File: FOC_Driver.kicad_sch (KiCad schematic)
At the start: 0 parts

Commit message: Wip
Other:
- removed sheet External_Power
- added sheet Encoder (Encoder.kicad_sch)
- added sheet External_Memory (External_Memory.kicad_sch)
- added sheet RS485 (RS485.kicad_sch)
- added sheet User_Interface (User_Interface.kicad_sch)
- sheet Connectors ports: added BypassRelay, Current_A, Current_B, Current_C, EM_STOP, PWM_AH, PWM_AL, PWM_BH, PWM_BL, PWM_CH, PWM_CL, SoftwareBrake, busVoltage, heatsinkTemperature; removed none
- sheet MCU ports: added BusVoltage, Bypass_Relay, Current_A, Current_B, Current_C, EM_STOP, Encoder_0, Encoder_A, Encoder_B, Encoder_En, Encoder_Flg, MISO, MOSI, RS485_Rx, RS485_Tx, SCLK, Software_Brake, heatsinkTemperature, nCS, nWP; removed none

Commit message: wip
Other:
- sheet Connectors ports: added Disable_Drive; removed EM_STOP
- sheet MCU ports: added Disable_Drive, ESTOP, PWM_AH, PWM_AL, PWM_BH, PWM_BL, PWM_CH, PWM_CL, RS485_DE; removed EM_STOP
- sheet RS485 ports: added RS485_DE; removed none

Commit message: wip
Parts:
- added TP1: TestPoint, TestPoint:TestPoint_Pad_D1.0mm, symbol Connector:TestPoint
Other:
- added sheet Power (Power.kicad_sch)

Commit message: 90% schematic first layout
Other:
- sheet External_Memory ports: added none; removed nWP
- sheet MCU ports: added ERROR_LED, ESTOP_LED, Error_Fixed, RUN_LED, RUN/STOP; removed nWP
- sheet User_Interface ports: added ERROR_LED, ESTOP_LED, Error_Fixed, Estop, RUN_LED, RUN/STOP; removed none
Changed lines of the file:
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@@
+	(wire
+		(pts
+			(xy 104.14 138.43) (xy 116.84 138.43)
+		)
+		(stroke
+			(width 0)
+			(type default)
+		)
+	)
 	(wire
 		(pts
@@
 	(wire
 		(pts
+			(xy 104.14 128.27) (xy 116.84 128.27)
+		)
+		(stroke
+			(width 0)
+			(type default)
+		)
+	)
+	(wire
+		(pts
 			(xy 160.02 85.09) (xy 182.88 85.09)
 		)
@@
 	(wire
 		(pts
-			(xy 160.02 133.35) (xy 182.88 133.35)
+			(xy 104.14 125.73) (xy 116.84 125.73)
 		)
 		(stroke
@@
 	(wire
 		(pts
+			(xy 104.14 140.97) (xy 116.84 140.97)
+		)
+		(stroke
+			(width 0)
+			(type default)
+		)
+	)
+	(wire
+		(pts
 			(xy 97.79 36.83) (xy 138.43 36.83)
 		)
@@
 	(wire
 		(pts
+			(xy 104.14 130.81) (xy 116.84 130.81)
+		)
+		(stroke
+			(width 0)
+			(type default)
+		)
+	)
+	(wire
+		(pts
 			(xy 97.79 46.99) (xy 128.27 46.99)
 		)
@@
 		(pts
 			(xy 102.87 87.63) (xy 116.84 87.63)
+		)
+		(stroke
+			(width 0)
+			(type default)
+		)
+	)
+	(wire
+		(pts
+			(xy 104.14 135.89) (xy 116.84 135.89)
 		)
 		(stroke
@@
 			)
 		)
-		(pin "nWP" input
-			(at 182.88 133.35 180)
-			(effects
-				(font
-					(size 1.27 1.27)
-				)
-				(justify left)
-			)
-		)
 		(pin "MISO" output
 			(at 182.88 135.89 180)
@@
 			)
 		)
-		(pin "nWP" output
-			(at 160.02 133.35 0)
-			(effects
-				(font
-					(size 1.27 1.27)
-				)
-				(justify right)
-			)
-		)
 		(pin "PWM_CH" output
 			(at 160.02 72.39 0)
@@
 		(pin "RS485_DE" output
 			(at 116.84 80.01 180)
+			(effects
+				(font
+					(size 1.27 1.27)
+				)
+				(justify left)
+			)
+		)
+		(pin "ERROR_LED" output
+			(at 116.84 125.73 180)
+			(effects
+				(font
+					(size 1.27 1.27)
+				)
+				(justify left)
+			)
+		)
+		(pin "RUN{slash}STOP" input
+			(at 116.84 138.43 180)
+			(effects
+				(font
+					(size 1.27 1.27)
+				)
+				(justify left)
+			)
+		)
+		(pin "ESTOP_LED" output
+			(at 116.84 130.81 180)
+			(effects
+				(font
+					(size 1.27 1.27)
+				)
+				(justify left)
+			)
+		)
+		(pin "RUN_LED" output
+			(at 116.84 128.27 180)
+			(effects
+				(font
+					(size 1.27 1.27)
+				)
+				(justify left)
+			)
+		)
+		(pin "Error_Fixed" input
+			(at 116.84 135.89 180)
 			(effects
 				(font
@@
 			)
 		)
+		(pin "Error_Fixed" output
+			(at 104.14 135.89 0)
+			(effects
+				(font
+					(size 1.27 1.27)
+				)
+				(justify right)
+			)
+		)
+		(pin "Estop" output
+			(at 104.14 140.97 0)
+			(effects
+				(font
+					(size 1.27 1.27)
+				)
+				(justify right)
+			)
+		)
+		(pin "RUN{slash}STOP" output
+			(at 104.14 138.43 0)
+			(effects
+				(font
+					(size 1.27 1.27)
+				)
+				(justify right)
+			)
+		)
+		(pin "ESTOP_LED" input
+			(at 104.14 130.81 0)
+			(effects
+				(font
+					(size 1.27 1.27)
+				)
+				(justify right)
+			)
+		)
+		(pin "RUN_LED" input
+			(at 104.14 128.27 0)
+			(effects
+				(font
+					(size 1.27 1.27)
+				)
+				(justify right)
+			)
+		)
+		(pin "ERROR_LED" input
+			(at 104.14 125.73 0)
+			(effects
+				(font
+					(size 1.27 1.27)
+				)
+				(justify right)
+			)
+		)

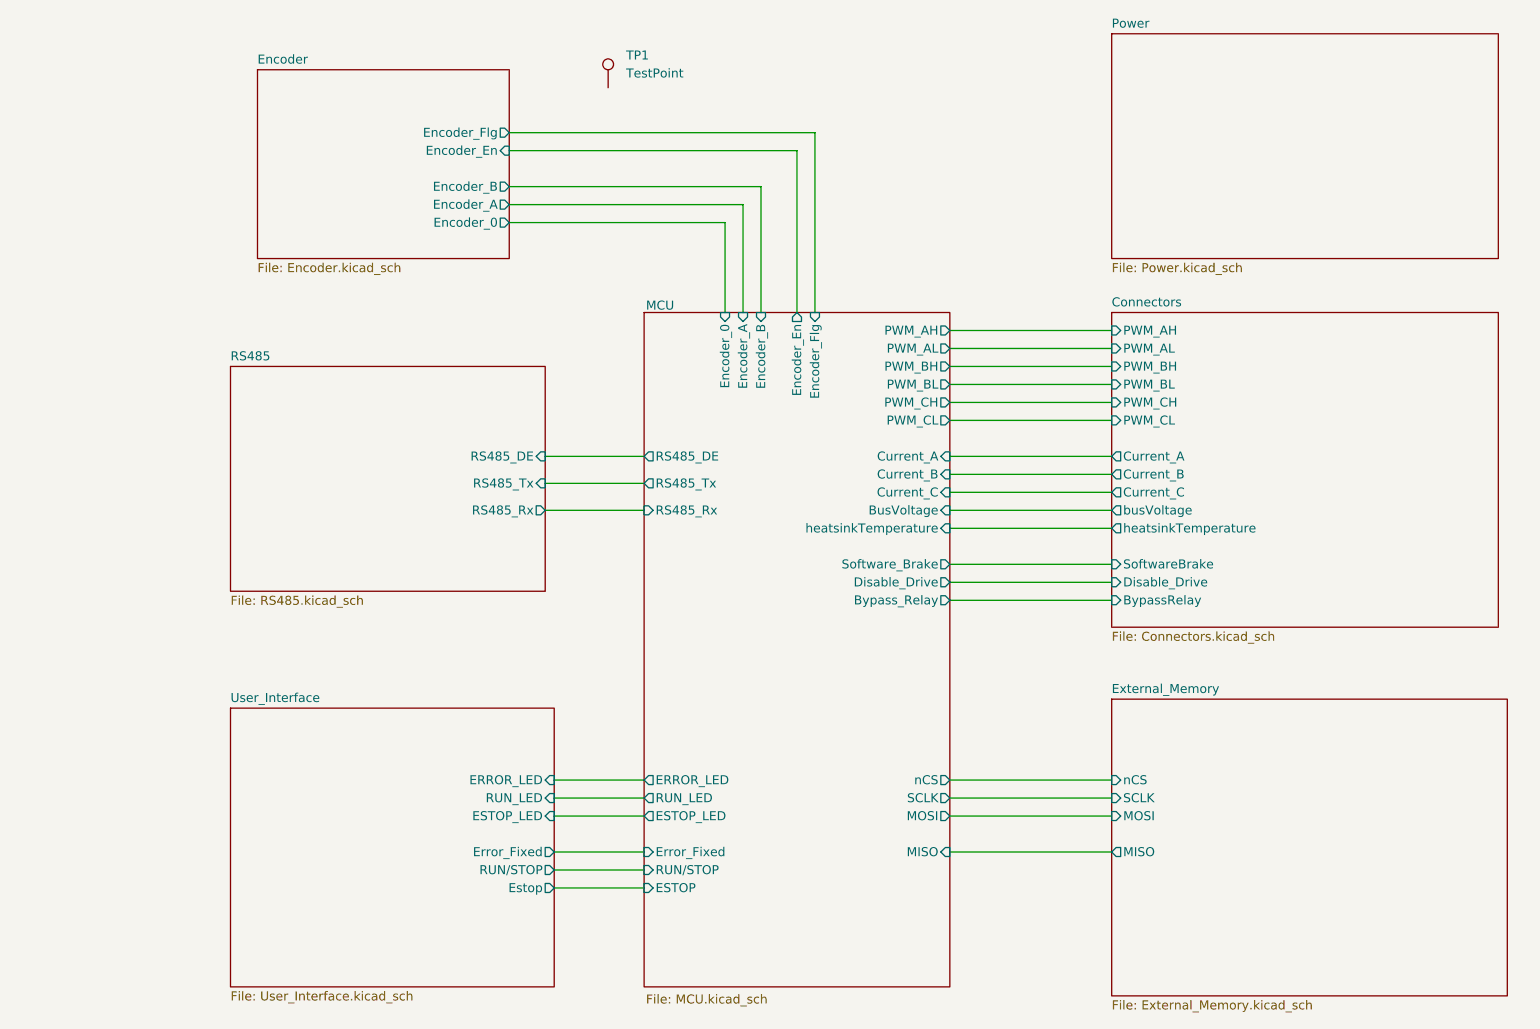
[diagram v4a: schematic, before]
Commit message: Addition of testpoints
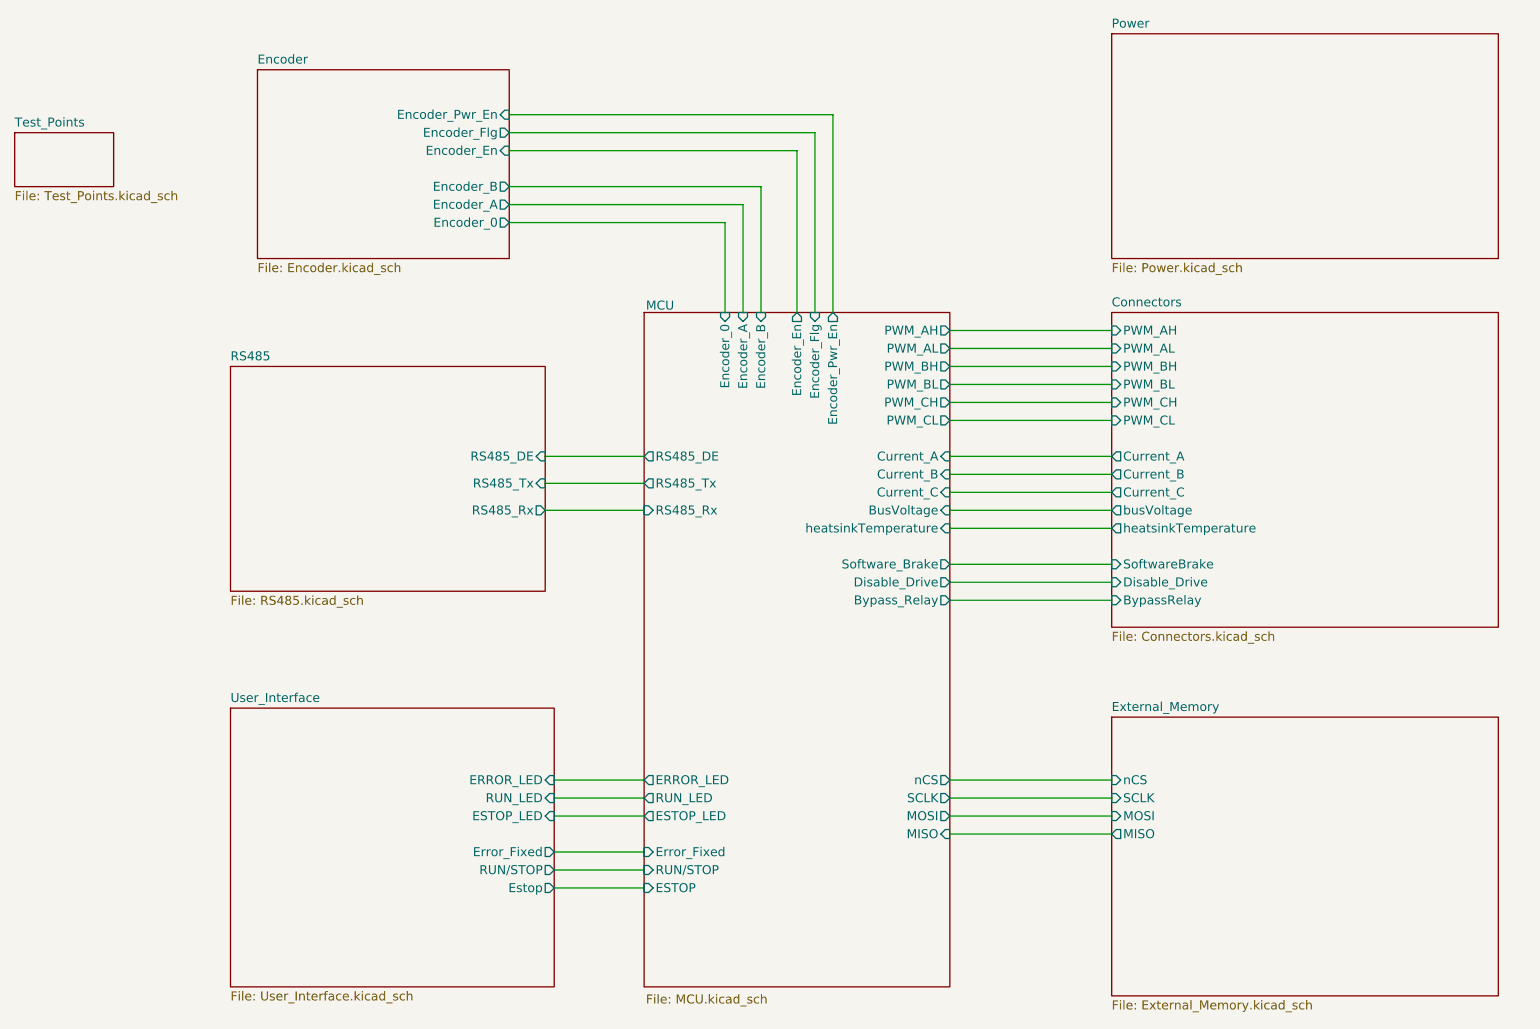
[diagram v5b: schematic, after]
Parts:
- removed TP1: TestPoint, TestPoint:TestPoint_Pad_D1.0mm, symbol Connector:TestPoint
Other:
- added sheet Test_Points (Test_Points.kicad_sch)
- sheet Encoder ports: added Encoder_Pwr_En; removed none
- sheet MCU ports: added Encoder_Pwr_En; removed none
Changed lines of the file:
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@@
+	(wire
+		(pts
+			(xy 160.02 133.35) (xy 182.88 133.35)
+		)
+		(stroke
+			(width 0)
+			(type default)
+		)
+	)
 	(wire
 		(pts
@@
 	(wire
 		(pts
+			(xy 143.51 31.75) (xy 143.51 59.69)
+		)
+		(stroke
+			(width 0)
+			(type default)
+		)
+	)
+	(wire
+		(pts
 			(xy 160.02 87.63) (xy 182.88 87.63)
 		)
@@
 	(wire
 		(pts
+			(xy 97.79 31.75) (xy 143.51 31.75)
+		)
+		(stroke
+			(width 0)
+			(type default)
+		)
+	)
+	(wire
+		(pts
 			(xy 104.14 140.97) (xy 116.84 140.97)
 		)
@@
 	(wire
 		(pts
-			(xy 160.02 135.89) (xy 182.88 135.89)
-		)
-		(stroke
-			(width 0)
-			(type default)
-		)
-	)
-	(wire
-		(pts
 			(xy 160.02 72.39) (xy 182.88 72.39)
 		)
@@
 		)
 	)
-	(symbol
-		(lib_id "Connector:TestPoint")
-		(at 111.76 27.94 0)
-		(unit 1)
+	(sheet
+		(at 182.88 116.84)
+		(size 54.61 39.37)
 		(exclude_from_sim no)
 		(in_bom yes)
@@
 		(dnp no)
 		(fields_autoplaced yes)
-		(property "Reference" "TP1"
-			(at 114.3 23.3679 0)
-			(effects
-				(font
-					(size 1.27 1.27)
-				)
-				(justify left)
-			)
-		)
-		(property "Value" "TestPoint"
-			(at 114.3 25.9079 0)
-			(effects
-				(font
-					(size 1.27 1.27)
-				)
-				(justify left)
-			)
-		)
-		(property "Footprint" "TestPoint:TestPoint_Pad_D1.0mm"
-			(at 116.84 27.94 0)
-			(effects
-				(font
-					(size 1.27 1.27)
-				)
-				(hide yes)
-			)
-		)
-		(property "Datasheet" "~"
-			(at 116.84 27.94 0)
-			(effects
-				(font
-					(size 1.27 1.27)
-				)
-				(hide yes)
-			)
-		)
-		(property "Description" "test point"
-			(at 111.76 27.94 0)
-			(effects
-				(font
-					(size 1.27 1.27)
-				)
-				(hide yes)
-			)
-		)
-		(pin "1"
-		)
-		(instances
-			(project ""
-				(path "/d122ff09-cd02-4f53-acb5-49b9ee3003a4"
-					(reference "TP1")
-					(unit 1)
-				)
-			)
-		)
-	)
-	(sheet
-		(at 182.88 114.3)
-		(size 55.88 41.91)
-		(exclude_from_sim no)
-		(in_bom yes)
-		(on_board yes)
-		(dnp no)
-		(fields_autoplaced yes)
 		(stroke
 			(width 0.1524)
@@
 		)
 		(fill
-			(color 0 0 0 0.0000)
+			(color 255 153 0 0.2000)
 		)
 		(property "Sheetname" "External_Memory"
-			(at 182.88 113.5884 0)
+			(at 182.88 116.1284 0)
 			(effects
 				(font
@@
 		)
 		(pin "MISO" output
-			(at 182.88 135.89 180)
+			(at 182.88 133.35 180)
 			(effects
 				(font
@@
 		)
 		(pin "MISO" input
-			(at 160.02 135.89 0)
+			(at 160.02 133.35 0)
 			(effects
 				(font
@@
 				)
 				(justify left)
+			)
+		)
+		(pin "Encoder_Pwr_En" output
+			(at 143.51 59.69 90)
+			(effects
+				(font
+					(size 1.27 1.27)
+				)
+				(justify right)
 			)
 		)
@@
 		)
 		(fill
-			(color 0 0 0 0.0000)
+			(color 255 255 0 0.2000)
 		)
 		(property "Sheetname" "Connectors"
@@
 		)
 		(fill
-			(color 0 0 0 0.0000)
+			(color 255 0 0 0.2000)
 		)
 		(property "Sheetname" "Power"
@@
 				(path "/d122ff09-cd02-4f53-acb5-49b9ee3003a4"
 					(page "8")
+				)
+			)
+		)
+	)
+	(sheet
+		(at 27.94 34.29)
+		(size 13.97 7.62)
+		(exclude_from_sim no)
+		(in_bom yes)
+		(on_board yes)
+		(dnp no)
+		(fields_autoplaced yes)
+		(stroke
+			(width 0.1524)
+			(type solid)
+		)
+		(fill
+			(color 0 0 0 0.0000)
+		)
+		(property "Sheetname" "Test_Points"
+			(at 27.94 33.5784 0)
+			(effects
+				(font
+					(size 1.27 1.27)
+				)
+				(justify left bottom)
+			)
+		)
+		(property "Sheetfile" "Test_Points.kicad_sch"
+			(at 27.94 42.4946 0)
+			(effects
+				(font
+					(size 1.27 1.27)
+				)
+				(justify left top)
+			)
+		)
+		(instances
+			(project "FOC_Driver"
+				(path "/d122ff09-cd02-4f53-acb5-49b9ee3003a4"
+					(page "9")
 				)
 			)
@@
 		)
 		(fill
-			(color 0 0 0 0.0000)
+			(color 0 255 255 0.2000)
 		)
 		(property "Sheetname" "Encoder"
@@
 		(pin "Encoder_Flg" output
 			(at 97.79 34.29 0)
+			(effects
+				(font
+					(size 1.27 1.27)
+				)
+				(justify right)
+			)
+		)
+		(pin "Encoder_Pwr_En" input
+			(at 97.79 31.75 0)
 			(effects
 				(font
@@
 		)
 		(fill
-			(color 0 0 0 0.0000)
+			(color 0 0 255 0.2000)
 		)
 		(property "Sheetname" "User_Interface"
@@
 		)
 		(fill
-			(color 0 0 0 0.0000)
+			(color 0 255 0 0.2000)
 		)
 		(property "Sheetname" "RS485"
